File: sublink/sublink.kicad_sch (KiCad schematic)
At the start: 45 parts, among them J1 ZL315-4SGH, Q1 Q_PMOS_GSD, SW1 SW_Push, SW2 SW_Push, SW3 SW_Push, U1 ATtiny414-SS, U2 OKY3402, U3 JS202011

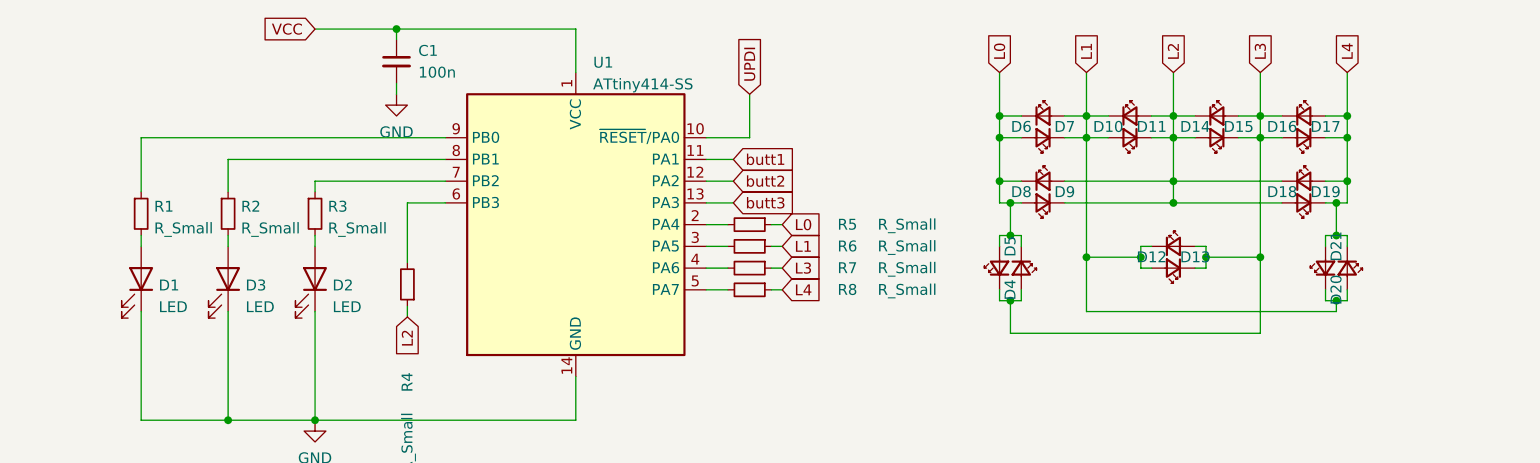
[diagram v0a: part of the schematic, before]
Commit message: more readable led numbering
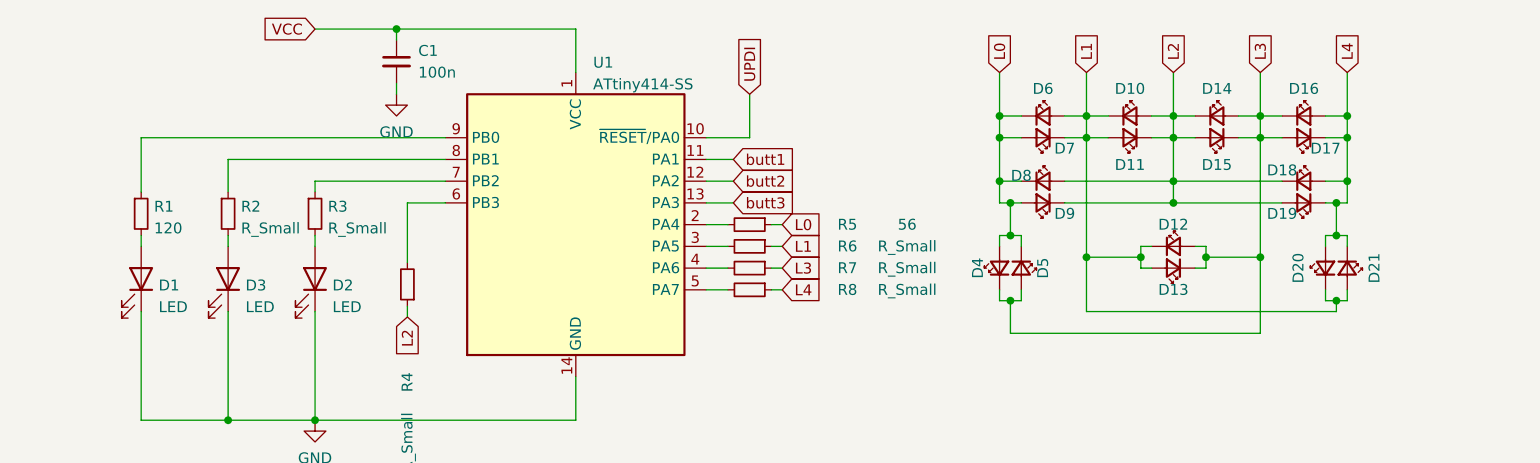
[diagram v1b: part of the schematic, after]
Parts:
- R1: value R_Small -> 120
- R5: value R_Small -> 56
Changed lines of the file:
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@@
   (symbol (lib_id "Device:LED_Small") (at 181.61 49.53 180) (unit 1)
     (in_bom yes) (on_board yes)
-    (property "Reference" "D9" (id 0) (at 184.15 48.26 0))
+    (property "Reference" "D9" (id 0) (at 184.15 50.8 0))
     (property "Value" "LED_Small" (id 1) (at 183.2487 47.752 90)
       (effects (font (size 1.27 1.27)) (justify right) hide)
@@
   (symbol (lib_id "Device:LED_Small") (at 191.77 41.91 180) (unit 1)
     (in_bom yes) (on_board yes)
-    (property "Reference" "D11" (id 0) (at 194.31 40.64 0))
+    (property "Reference" "D11" (id 0) (at 191.77 45.085 0))
     (property "Value" "LED_Small" (id 1) (at 193.4087 40.132 90)
       (effects (font (size 1.27 1.27)) (justify right) hide)
@@
   (symbol (lib_id "Device:LED_Small") (at 201.93 41.91 180) (unit 1)
     (in_bom yes) (on_board yes)
-    (property "Reference" "D15" (id 0) (at 204.47 40.64 0))
+    (property "Reference" "D15" (id 0) (at 201.93 45.085 0))
     (property "Value" "LED_Small" (id 1) (at 203.5687 40.132 90)
       (effects (font (size 1.27 1.27)) (justify right) hide)
@@
   (symbol (lib_id "Device:LED_Small") (at 176.53 57.15 90) (unit 1)
     (in_bom yes) (on_board yes)
-    (property "Reference" "D4" (id 0) (at 177.8 59.69 0))
+    (property "Reference" "D4" (id 0) (at 173.99 57.15 0))
     (property "Value" "LED_Small" (id 1) (at 178.308 58.7887 90)
       (effects (font (size 1.27 1.27)) (justify right) hide)
@@
   (symbol (lib_id "Device:LED_Small") (at 201.93 39.37 0) (unit 1)
     (in_bom yes) (on_board yes)
-    (property "Reference" "D14" (id 0) (at 199.39 40.64 0))
+    (property "Reference" "D14" (id 0) (at 201.93 36.195 0))
     (property "Value" "LED_Small" (id 1) (at 200.2913 41.148 90)
       (effects (font (size 1.27 1.27)) (justify right) hide)
@@
   (symbol (lib_id "Device:LED_Small") (at 212.09 46.99 0) (unit 1)
     (in_bom yes) (on_board yes)
-    (property "Reference" "D18" (id 0) (at 209.55 48.26 0))
+    (property "Reference" "D18" (id 0) (at 209.55 45.72 0))
     (property "Value" "LED_Small" (id 1) (at 210.4513 48.768 90)
       (effects (font (size 1.27 1.27)) (justify right) hide)
@@
   (symbol (lib_id "Device:LED_Small") (at 179.07 57.15 270) (unit 1)
     (in_bom yes) (on_board yes)
-    (property "Reference" "D5" (id 0) (at 177.8 54.61 0))
+    (property "Reference" "D5" (id 0) (at 181.61 57.15 0))
     (property "Value" "LED_Small" (id 1) (at 177.292 55.5113 90)
       (effects (font (size 1.27 1.27)) (justify right) hide)
@@
       (effects (font (size 1.27 1.27)) (justify left))
     )
-    (property "Value" "R_Small" (id 1) (at 77.6986 52.5022 0)
+    (property "Value" "120" (id 1) (at 77.6986 52.5022 0)
       (effects (font (size 1.27 1.27)) (justify left))
     )
@@
   (symbol (lib_id "Device:LED_Small") (at 212.09 39.37 0) (unit 1)
     (in_bom yes) (on_board yes)
-    (property "Reference" "D16" (id 0) (at 209.55 40.64 0))
+    (property "Reference" "D16" (id 0) (at 212.09 36.195 0))
     (property "Value" "LED_Small" (id 1) (at 210.4513 41.148 90)
       (effects (font (size 1.27 1.27)) (justify right) hide)
@@
   (symbol (lib_id "Device:LED_Small") (at 196.85 54.61 0) (unit 1)
     (in_bom yes) (on_board yes)
-    (property "Reference" "D12" (id 0) (at 194.31 55.88 0))
+    (property "Reference" "D12" (id 0) (at 196.85 52.07 0))
     (property "Value" "LED_Small" (id 1) (at 195.2113 56.388 90)
       (effects (font (size 1.27 1.27)) (justify right) hide)
@@
   (symbol (lib_id "Device:LED_Small") (at 181.61 46.99 0) (unit 1)
     (in_bom yes) (on_board yes)
-    (property "Reference" "D8" (id 0) (at 179.07 48.26 0))
+    (property "Reference" "D8" (id 0) (at 179.07 46.355 0))
     (property "Value" "LED_Small" (id 1) (at 179.9713 48.768 90)
       (effects (font (size 1.27 1.27)) (justify right) hide)
@@
   (symbol (lib_id "Device:LED_Small") (at 181.61 41.91 180) (unit 1)
     (in_bom yes) (on_board yes)
-    (property "Reference" "D7" (id 0) (at 184.15 40.64 0))
+    (property "Reference" "D7" (id 0) (at 184.15 43.18 0))
     (property "Value" "LED_Small" (id 1) (at 183.2487 40.132 90)
       (effects (font (size 1.27 1.27)) (justify right) hide)
@@
   (symbol (lib_id "Device:LED_Small") (at 212.09 49.53 180) (unit 1)
     (in_bom yes) (on_board yes)
-    (property "Reference" "D19" (id 0) (at 214.63 48.26 0))
+    (property "Reference" "D19" (id 0) (at 209.55 50.8 0))
     (property "Value" "LED_Small" (id 1) (at 213.7287 47.752 90)
       (effects (font (size 1.27 1.27)) (justify right) hide)
@@
   (symbol (lib_id "Device:LED_Small") (at 214.63 57.15 90) (unit 1)
     (in_bom yes) (on_board yes)
-    (property "Reference" "D20" (id 0) (at 215.9 59.69 0))
+    (property "Reference" "D20" (id 0) (at 211.455 57.15 0))
     (property "Value" "LED_Small" (id 1) (at 216.408 58.7887 90)
       (effects (font (size 1.27 1.27)) (justify right) hide)
@@
   (symbol (lib_id "Device:LED_Small") (at 217.17 57.15 270) (unit 1)
     (in_bom yes) (on_board yes)
-    (property "Reference" "D21" (id 0) (at 215.9 54.61 0))
+    (property "Reference" "D21" (id 0) (at 220.345 57.15 0))
     (property "Value" "LED_Small" (id 1) (at 215.392 55.5113 90)
       (effects (font (size 1.27 1.27)) (justify right) hide)
@@
   (symbol (lib_id "Device:LED_Small") (at 212.09 41.91 180) (unit 1)
     (in_bom yes) (on_board yes)
-    (property "Reference" "D17" (id 0) (at 214.63 40.64 0))
+    (property "Reference" "D17" (id 0) (at 214.63 43.18 0))
     (property "Value" "LED_Small" (id 1) (at 213.7287 40.132 90)
       (effects (font (size 1.27 1.27)) (justify right) hide)
@@
     (in_bom yes) (on_board yes)
     (property "Reference" "R5" (id 0) (at 158.75 52.07 90))
-    (property "Value" "R_Small" (id 1) (at 165.735 52.07 90))
+    (property "Value" "56" (id 1) (at 165.735 52.07 90))
     (property "Footprint" "Resistor_SMD:R_0805_2012Metric_Pad1.20x1.40mm_HandSolder" (id 2) (at 147.32 52.07 0)
       (effects (font (size 1.27 1.27)) hide)
@@
   (symbol (lib_id "Device:LED_Small") (at 181.61 39.37 0) (unit 1)
     (in_bom yes) (on_board yes)
-    (property "Reference" "D6" (id 0) (at 179.07 40.64 0))
+    (property "Reference" "D6" (id 0) (at 181.61 36.195 0))
     (property "Value" "LED_Small" (id 1) (at 179.9713 41.148 90)
       (effects (font (size 1.27 1.27)) (justify right) hide)
@@
   (symbol (lib_id "Device:LED_Small") (at 196.85 57.15 180) (unit 1)
     (in_bom yes) (on_board yes)
-    (property "Reference" "D13" (id 0) (at 199.39 55.88 0))
+    (property "Reference" "D13" (id 0) (at 196.85 59.69 0))
     (property "Value" "LED_Small" (id 1) (at 198.4887 55.372 90)
       (effects (font (size 1.27 1.27)) (justify right) hide)
@@
   (symbol (lib_id "Device:LED_Small") (at 191.77 39.37 0) (unit 1)
     (in_bom yes) (on_board yes)
-    (property "Reference" "D10" (id 0) (at 189.23 40.64 0))
+    (property "Reference" "D10" (id 0) (at 191.77 36.195 0))
     (property "Value" "LED_Small" (id 1) (at 190.1313 41.148 90)
       (effects (font (size 1.27 1.27)) (justify right) hide)
@@
     )
     (path "/480cfc26-2c62-4bd8-bba1-ebc5c356850c"
-      (reference "R1") (unit 1) (value "R_Small") (footprint "Resistor_SMD:R_0805_2012Metric_Pad1.20x1.40mm_HandSolder")
+      (reference "R1") (unit 1) (value "120") (footprint "Resistor_SMD:R_0805_2012Metric_Pad1.20x1.40mm_HandSolder")
     )
     (path "/421cbe80-8cf3-4d46-abc1-47a35219073c"
@@
     )
     (path "/b390f734-480e-4efb-bb88-3455ace2453a"
-      (reference "R5") (unit 1) (value "R_Small") (footprint "Resistor_SMD:R_0805_2012Metric_Pad1.20x1.40mm_HandSolder")
+      (reference "R5") (unit 1) (value "56") (footprint "Resistor_SMD:R_0805_2012Metric_Pad1.20x1.40mm_HandSolder")
     )
     (path "/32202941-5c41-4fde-86ab-99df39fda948"
